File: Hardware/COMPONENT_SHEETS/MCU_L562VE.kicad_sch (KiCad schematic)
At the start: 33 parts, among them IC1 STM32L562ZET6, SW1 MCU Reset, Y3 32MHz

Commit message: Rerouted some stuffs, close to final for Rev 3
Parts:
- R12: footprint Resistor_SMD:R_0201_0603Metric_Pad0.64x0.40mm_HandSolder -> Resistor_SMD:R_0603_1608Metric_Pad0.98x0.95mm_HandSolder
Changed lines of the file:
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@@
     (property "Reference" "R12" (id 0) (at 56.515 22.86 0))
     (property "Value" "4.7k" (id 1) (at 56.515 25.4 0))
-    (property "Footprint" "Resistor_SMD:R_0201_0603Metric_Pad0.64x0.40mm_HandSolder" (id 2) (at 59.69 25.4 0)
+    (property "Footprint" "Resistor_SMD:R_0603_1608Metric_Pad0.98x0.95mm_HandSolder" (id 2) (at 59.69 25.4 0)
       (effects (font (size 1.27 1.27)) hide)
     )

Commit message: Updated LCSC numbers and cleaned up routing
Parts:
- C24, C25: LCSC C400083 -> C123555
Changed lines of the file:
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@@
       (effects (font (size 1.27 1.27)) hide)
     )
-    (property "LCSC" "C400083" (id 4) (at 43.18 106.68 0)
+    (property "LCSC" "C123555" (id 4) (at 43.18 106.68 0)
       (effects (font (size 1.27 1.27)) hide)
     )
@@
       (effects (font (size 1.27 1.27)) hide)
     )
-    (property "LCSC" "C400083" (id 4) (at 33.02 106.68 0)
+    (property "LCSC" "C123555" (id 4) (at 33.02 106.68 0)
       (effects (font (size 1.27 1.27)) hide)
     )

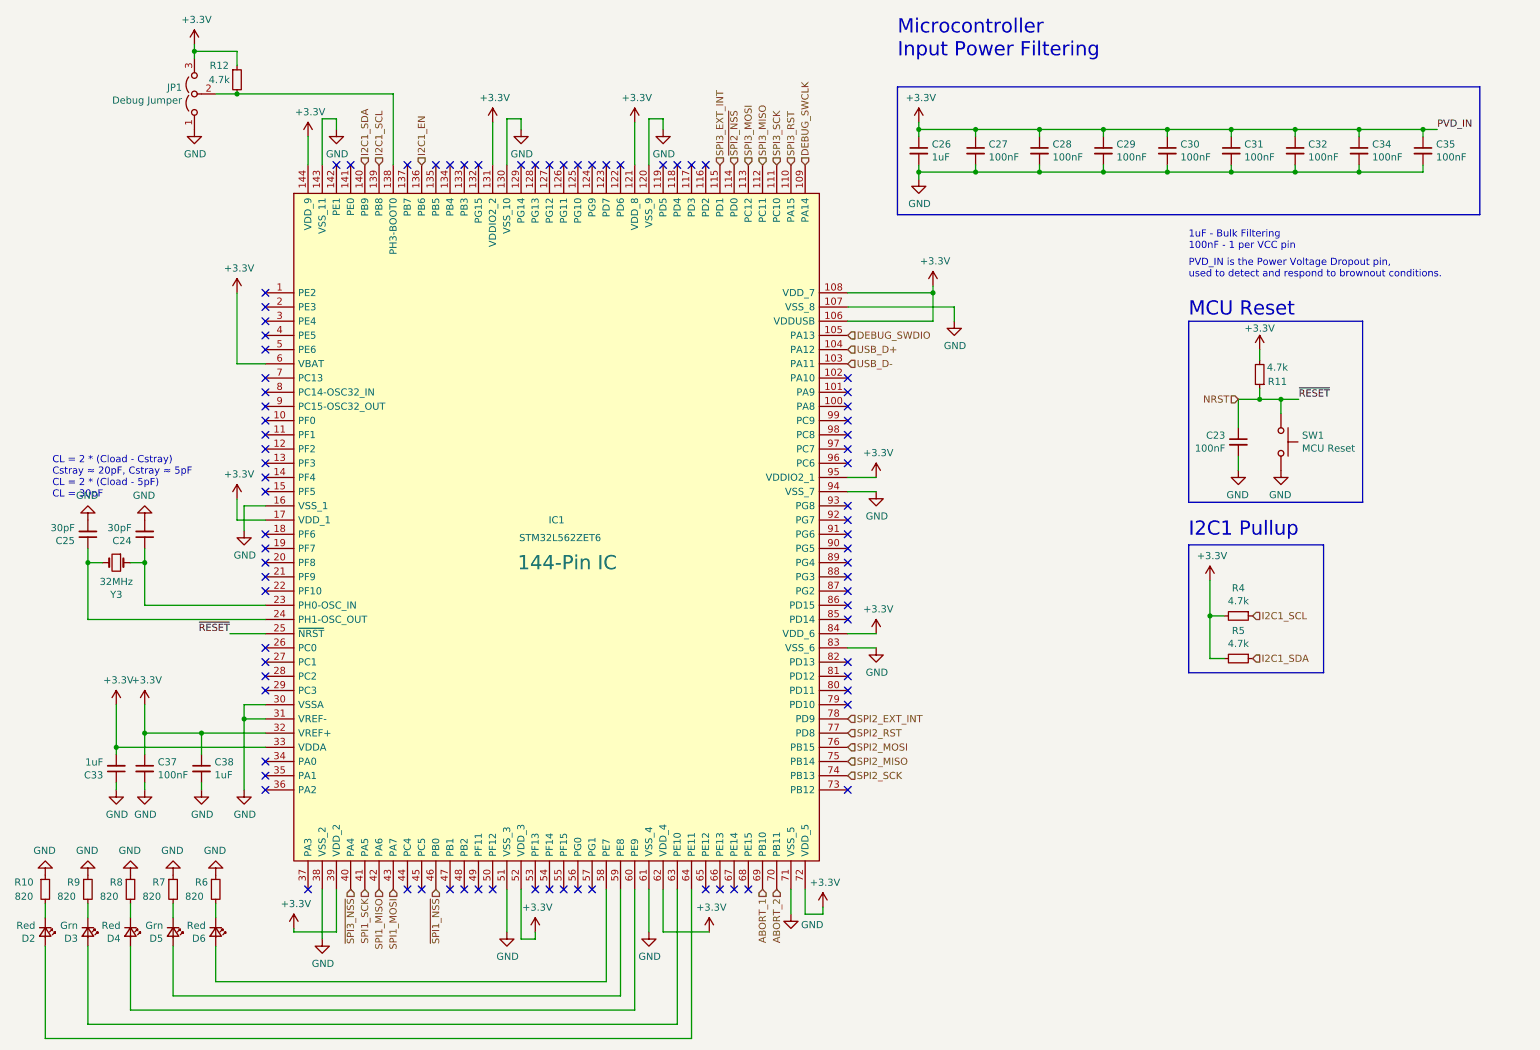
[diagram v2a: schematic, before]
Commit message: Updated LCSC numbers, updated BOM file, added power LED.
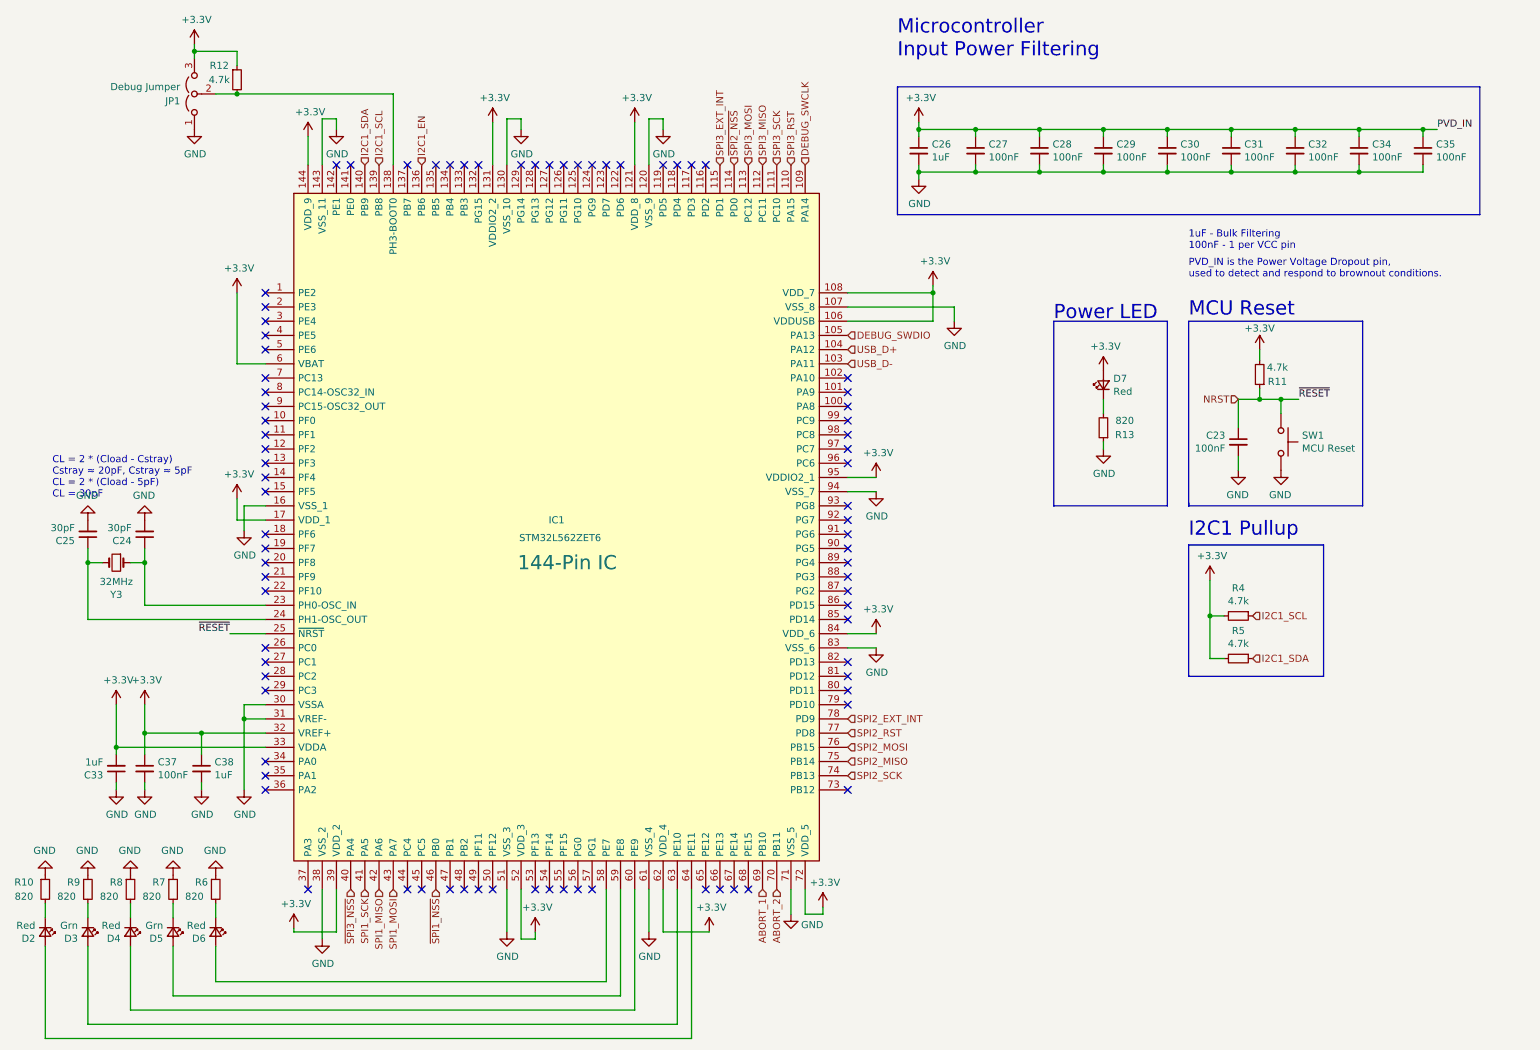
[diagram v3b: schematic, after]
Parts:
- added D7: Red, LED_SMD:LED_0603_1608Metric_Pad1.05x0.95mm_HandSolder, symbol Device:LED_Small
- added R13: 820, Resistor_SMD:R_0603_1608Metric, symbol Device:R_Small
- D3, D5: LCSC C138548 -> C434423
- JP1: LCSC (none) -> C5346215
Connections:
- net +3V3: now also D7.2 (A)
- net GND: now also R13.1
- new net: D7.1 (K), R13.2
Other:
- note added: "Power LED"
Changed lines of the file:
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@@
     (stroke (width 0) (type default) (color 0 0 0 0))
   )
-  (polyline (pts (xy 229.87 100.965) (xy 260.985 100.965))
+  (polyline (pts (xy 229.87 101.6) (xy 260.985 101.6))
     (stroke (width 0) (type default) (color 0 0 0 0))
   )
@@
     (stroke (width 0) (type default) (color 0 0 0 0))
   )
+  (wire (pts (xy 214.63 82.55) (xy 214.63 85.09))
+    (stroke (width 0) (type default) (color 0 0 0 0))
+  )
   (wire (pts (xy 59.69 104.14) (xy 64.77 104.14))
     (stroke (width 0) (type default) (color 0 0 0 0))
@@
     (stroke (width 0) (type default) (color 0 0 0 0))
   )
-  (polyline (pts (xy 260.985 68.58) (xy 260.985 100.965))
+  (polyline (pts (xy 260.985 68.58) (xy 260.985 101.6))
     (stroke (width 0) (type default) (color 0 0 0 0))
   )
@@
     (stroke (width 0) (type default) (color 0 0 0 0))
   )
+  (polyline (pts (xy 205.74 101.6) (xy 226.06 101.6))
+    (stroke (width 0) (type default) (color 0 0 0 0))
+  )
   (wire (pts (xy 226.06 41.91) (xy 237.49 41.91))
     (stroke (width 0) (type default) (color 0 0 0 0))
@@
     (stroke (width 0) (type default) (color 0 0 0 0))
   )
-  (polyline (pts (xy 229.87 100.965) (xy 229.87 68.58))
+  (polyline (pts (xy 229.87 101.6) (xy 229.87 68.58))
     (stroke (width 0) (type default) (color 0 0 0 0))
   )
@@
     (stroke (width 0) (type default) (color 0 0 0 0))
   )
-  (polyline (pts (xy 229.87 131.445) (xy 229.87 108.585))
+  (polyline (pts (xy 229.87 132.08) (xy 229.87 108.585))
     (stroke (width 0) (type default) (color 0 0 0 0))
   )
@@
     (stroke (width 0) (type default) (color 0 0 0 0))
   )
+  (wire (pts (xy 214.63 91.44) (xy 214.63 90.17))
+    (stroke (width 0) (type default) (color 0 0 0 0))
+  )
   (wire (pts (xy 87.63 27.94) (xy 87.63 40.64))
     (stroke (width 0) (type default) (color 0 0 0 0))
@@
     (stroke (width 0) (type default) (color 0 0 0 0))
   )
-  (polyline (pts (xy 254 131.445) (xy 229.87 131.445))
+  (polyline (pts (xy 254 132.08) (xy 229.87 132.08))
     (stroke (width 0) (type default) (color 0 0 0 0))
   )
@@
     (stroke (width 0) (type default) (color 0 0 0 0))
   )
-  (polyline (pts (xy 254 108.585) (xy 254 131.445))
+  (polyline (pts (xy 205.74 101.6) (xy 205.74 68.58))
+    (stroke (width 0) (type default) (color 0 0 0 0))
+  )
+  (polyline (pts (xy 254 108.585) (xy 254 132.08))
     (stroke (width 0) (type default) (color 0 0 0 0))
   )
@@
     (stroke (width 0) (type default) (color 0 0 0 0))
   )
+  (polyline (pts (xy 205.74 68.58) (xy 226.06 68.58))
+    (stroke (width 0) (type default) (color 0 0 0 0))
+  )
   (wire (pts (xy 181.61 43.18) (xy 181.61 41.91))
     (stroke (width 0) (type default) (color 0 0 0 0))
@@
     (stroke (width 0) (type default) (color 0 0 0 0))
   )
-  (polyline (pts (xy 229.87 100.965) (xy 229.87 100.965))
+  (polyline (pts (xy 229.87 101.6) (xy 229.87 100.965))
     (stroke (width 0) (type default) (color 0 0 0 0))
   )
@@
   )
   (wire (pts (xy 38.1 146.05) (xy 38.1 144.78))
+    (stroke (width 0) (type default) (color 0 0 0 0))
+  )
+  (polyline (pts (xy 226.06 101.6) (xy 226.06 68.58))
     (stroke (width 0) (type default) (color 0 0 0 0))
   )
@@
     (effects (font (size 1.27 1.27)) (justify left bottom))
   )
+  (text "Power LED\n" (at 205.74 68.58 0)
+    (effects (font (size 2.54 2.54)) (justify left bottom))
+  )
   (text "CL = 2 * (Cload - Cstray)\nCstray ≈ 20pF, Cstray ≈ 5pF\nCL = 2 * (Cload - 5pF)\nCL = 30pF"
     (at 26.67 100.33 0)
@@
       (effects (font (size 1.27 1.27)) hide)
     )
-    (property "LCSC" "C138548" (id 4) (at 33.02 177.8 90)
+    (property "LCSC" "C434423" (id 4) (at 33.02 177.8 90)
       (effects (font (size 1.27 1.27)) hide)
     )
@@
       (effects (font (size 1.27 1.27)) hide)
     )
-    (property "LCSC" "C138548" (id 4) (at 48.26 177.8 90)
+    (property "LCSC" "C434423" (id 4) (at 48.26 177.8 90)
       (effects (font (size 1.27 1.27)) hide)
     )
@@
   (symbol (lib_id "Jumper:Jumper_3_Open") (at 52.07 27.94 90) (unit 1)
     (in_bom yes) (on_board yes)
-    (property "Reference" "JP1" (id 0) (at 49.8602 26.7716 90)
-      (effects (font (size 1.27 1.27)) (justify left))
-    )
-    (property "Value" "Debug Jumper" (id 1) (at 49.8602 29.083 90)
+    (property "Reference" "JP1" (id 0) (at 49.53 29.21 90)
+      (effects (font (size 1.27 1.27)) (justify left))
+    )
+    (property "Value" "Debug Jumper" (id 1) (at 49.53 26.67 90)
       (effects (font (size 1.27 1.27)) (justify left))
     )
@@
     )
     (property "Datasheet" "~" (id 3) (at 52.07 27.94 0)
+      (effects (font (size 1.27 1.27)) hide)
+    )
+    (property "LCSC" "C5346215" (id 4) (at 52.07 27.94 0)
       (effects (font (size 1.27 1.27)) hide)
     )
@@
     (pin "1")
   )
+  (symbol (lib_id "power:GND") (at 214.63 91.44 0) (unit 1)
+    (in_bom yes) (on_board yes)
+    (property "Reference" "#PWR049" (id 0) (at 214.63 97.79 0)
+      (effects (font (size 1.27 1.27)) hide)
+    )
+    (property "Value" "GND" (id 1) (at 214.757 95.8342 0))
+    (property "Footprint" "" (id 2) (at 214.63 91.44 0)
+      (effects (font (size 1.27 1.27)) hide)
+    )
+    (property "Datasheet" "" (id 3) (at 214.63 91.44 0)
+      (effects (font (size 1.27 1.27)) hide)
+    )
+    (pin "1")
+  )
   (symbol (lib_id "Device:R_Small") (at 59.69 25.4 0) (unit 1)
     (in_bom yes) (on_board yes)
@@
     (pin "1")
   )
+  (symbol (lib_id "Device:R_Small") (at 214.63 87.63 180) (unit 1)
+    (in_bom yes) (on_board yes)
+    (property "Reference" "R13" (id 0) (at 218.44 88.9 0))
+    (property "Value" "820" (id 1) (at 218.44 86.36 0))
+    (property "Footprint" "Resistor_SMD:R_0603_1608Metric" (id 2) (at 214.63 87.63 0)
+      (effects (font (size 1.27 1.27)) hide)
+    )
+    (property "Datasheet" "~" (id 3) (at 214.63 87.63 0)
+      (effects (font (size 1.27 1.27)) hide)
+    )
+    (property "LCSC" " C23253 " (id 4) (at 214.63 87.63 0)
+      (effects (font (size 1.27 1.27)) hide)
+    )
+    (pin "1")
+    (pin "2")
+  )
   (symbol (lib_id "power:+3.3V") (at 72.39 35.56 0) (unit 1)
     (in_bom yes) (on_board yes)
@@
     (pin "1")
   )
+  (symbol (lib_id "power:+3.3V") (at 214.63 77.47 0) (unit 1)
+    (in_bom yes) (on_board yes)
+    (property "Reference" "#PWR048" (id 0) (at 214.63 81.28 0)
+      (effects (font (size 1.27 1.27)) hide)
+    )
+    (property "Value" "+3.3V" (id 1) (at 215.011 73.0758 0))
+    (property "Footprint" "" (id 2) (at 214.63 77.47 0)
+      (effects (font (size 1.27 1.27)) hide)
+    )
+    (property "Datasheet" "" (id 3) (at 214.63 77.47 0)
+      (effects (font (size 1.27 1.27)) hide)
+    )
+    (pin "1")
+  )
   (symbol (lib_id "power:+3.3V") (at 59.69 100.33 0) (unit 1)
     (in_bom yes) (on_board yes)
@@
     (pin "1")
   )
+  (symbol (lib_id "Device:LED_Small") (at 214.63 80.01 90) (unit 1)
+    (in_bom yes) (on_board yes)
+    (property "Reference" "D7" (id 0) (at 216.408 78.8416 90)
+      (effects (font (size 1.27 1.27)) (justify right))
+    )
+    (property "Value" "Red" (id 1) (at 216.408 81.153 90)
+      (effects (font (size 1.27 1.27)) (justify right))
+    )
+    (property "Footprint" "LED_SMD:LED_0603_1608Metric_Pad1.05x0.95mm_HandSolder" (id 2) (at 214.63 80.01 90)
+      (effects (font (size 1.27 1.27)) hide)
+    )
+    (property "Datasheet" "~" (id 3) (at 214.63 80.01 90)
+      (effects (font (size 1.27 1.27)) hide)
+    )
+    (property "LCSC" " C2286 " (id 4) (at 214.63 80.01 90)
+      (effects (font (size 1.27 1.27)) hide)
+    )
+    (pin "1")
+    (pin "2")
+  )
   (symbol (lib_id "power:+3.3V") (at 69.85 177.165 0) (unit 1)

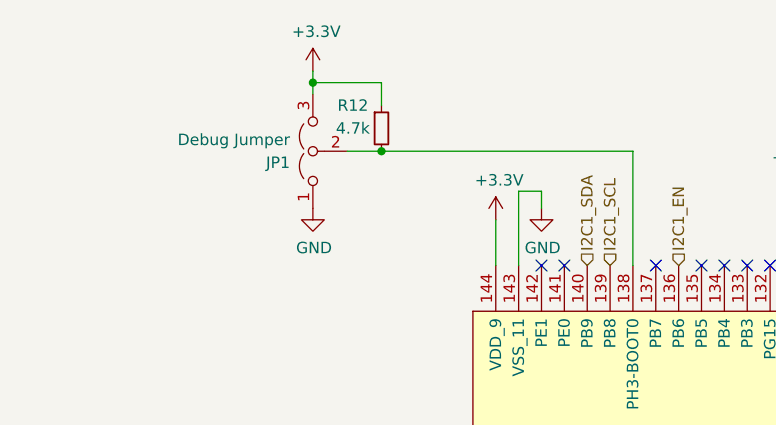
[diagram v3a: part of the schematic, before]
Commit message: Routed JTAG connector and set boot0 default to GND
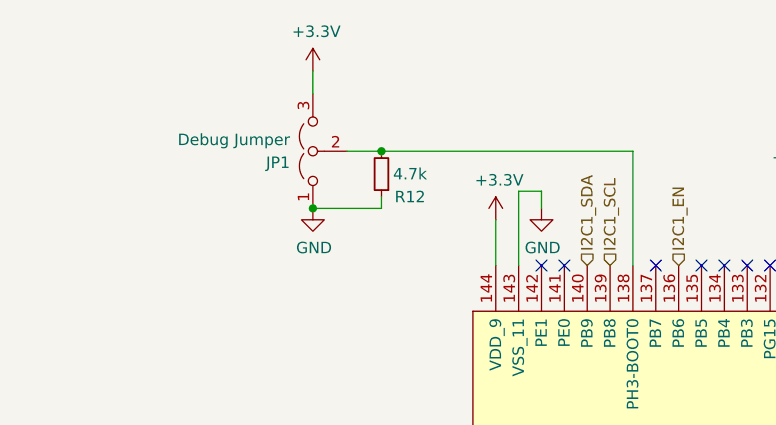
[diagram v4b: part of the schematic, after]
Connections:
- net +3V3: no longer R12.1
- net GND: now also R12.1
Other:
- moved on the sheet: R12
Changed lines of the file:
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@@
   (junction (at 248.92 41.91) (diameter 0) (color 0 0 0 0)
   )
-  (junction (at 52.07 20.32) (diameter 0) (color 0 0 0 0)
-  )
   (junction (at 242.57 82.55) (diameter 0) (color 0 0 0 0)
   )
@@
   )
   (junction (at 233.68 121.285) (diameter 0) (color 0 0 0 0)
+  )
+  (junction (at 52.07 34.29) (diameter 0) (color 0 0 0 0)
   )
   (junction (at 191.77 41.91) (diameter 0) (color 0 0 0 0)
@@
     (stroke (width 0) (type default) (color 0 0 0 0))
   )
+  (wire (pts (xy 52.07 34.29) (xy 59.69 34.29))
+    (stroke (width 0) (type default) (color 0 0 0 0))
+  )
   (wire (pts (xy 55.88 186.69) (xy 125.73 186.69))
     (stroke (width 0) (type default) (color 0 0 0 0))
@@
     (stroke (width 0) (type default) (color 0 0 0 0))
   )
-  (wire (pts (xy 52.07 20.32) (xy 52.07 21.59))
-    (stroke (width 0) (type default) (color 0 0 0 0))
-  )
   (wire (pts (xy 214.63 82.55) (xy 214.63 85.09))
     (stroke (width 0) (type default) (color 0 0 0 0))
@@
     (stroke (width 0) (type default) (color 0 0 0 0))
   )
-  (wire (pts (xy 59.69 20.32) (xy 52.07 20.32))
+  (wire (pts (xy 59.69 33.02) (xy 59.69 34.29))
     (stroke (width 0) (type default) (color 0 0 0 0))
   )
@@
     (stroke (width 0) (type default) (color 0 0 0 0))
   )
-  (wire (pts (xy 59.69 22.86) (xy 59.69 20.32))
-    (stroke (width 0) (type default) (color 0 0 0 0))
-  )
   (wire (pts (xy 135.89 177.8) (xy 144.145 177.8))
     (stroke (width 0) (type default) (color 0 0 0 0))
@@
     (stroke (width 0) (type default) (color 0 0 0 0))
   )
-  (wire (pts (xy 52.07 19.05) (xy 52.07 20.32))
+  (wire (pts (xy 52.07 19.05) (xy 52.07 21.59))
     (stroke (width 0) (type default) (color 0 0 0 0))
   )
@@
     (pin "1")
   )
-  (symbol (lib_id "Device:R_Small") (at 59.69 25.4 0) (unit 1)
-    (in_bom yes) (on_board yes)
-    (property "Reference" "R12" (id 0) (at 56.515 22.86 0))
-    (property "Value" "4.7k" (id 1) (at 56.515 25.4 0))
-    (property "Footprint" "Resistor_SMD:R_0603_1608Metric_Pad0.98x0.95mm_HandSolder" (id 2) (at 59.69 25.4 0)
-      (effects (font (size 1.27 1.27)) hide)
-    )
-    (property "Datasheet" "~" (id 3) (at 59.69 25.4 0)
-      (effects (font (size 1.27 1.27)) hide)
-    )
-    (property "LCSC" "C25999" (id 4) (at 59.69 25.4 90)
-      (effects (font (size 1.27 1.27)) hide)
-    )
+  (symbol (lib_id "Device:R_Small") (at 59.69 30.48 180) (unit 1)
+    (in_bom yes) (on_board yes)
+    (property "Reference" "R12" (id 0) (at 62.865 33.02 0))
+    (property "Value" "4.7k" (id 1) (at 62.865 30.48 0))
+    (property "Footprint" "Resistor_SMD:R_0603_1608Metric_Pad0.98x0.95mm_HandSolder" (id 2) (at 59.69 30.48 0)
+      (effects (font (size 1.27 1.27)) hide)
+    )
+    (property "Datasheet" "~" (id 3) (at 59.69 30.48 0)
+      (effects (font (size 1.27 1.27)) hide)
+    )
+    (property "LCSC" "C25999" (id 4) (at 59.69 30.48 90)
+      (effects (font (size 1.27 1.27)) hide)
+    )
